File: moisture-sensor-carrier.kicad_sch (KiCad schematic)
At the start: 60 parts, among them J1 USB-C receptacle, J2 Battery - Adafruit 1578, J3 Solar panel, J4 SWD 10p 1.27mm, J5 U.FL-R-SMT-1(10) antenna, U1 nRF54L15-QFAA, U2 nPM1300-QEAA, U3 FDC1004, U4 SHT45-AD1F, U5 TPS7A1650 5V LDO, X1 CM8V-T1A 32.768kHz CL=7pF 20p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, X2 FA-128 32MHz CL=8pF

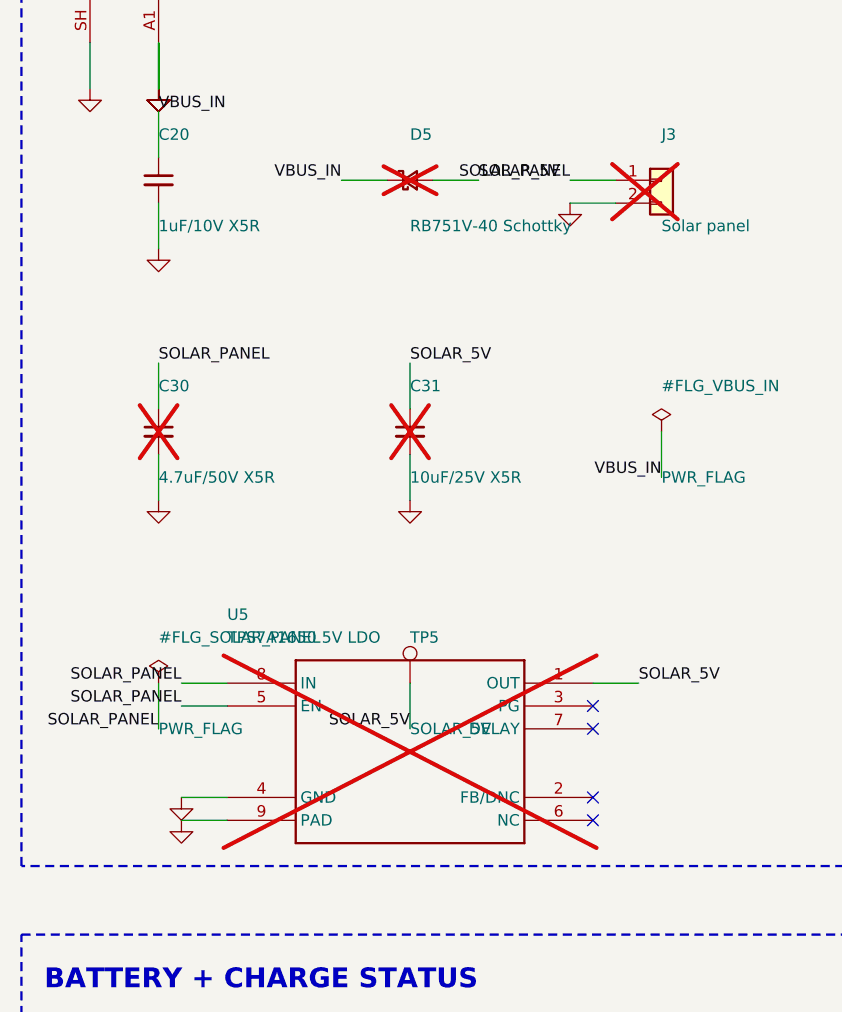
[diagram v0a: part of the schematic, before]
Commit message: Place U5/C30/C31 in the solar reserve; solar is populated on every board
Two changes.

SOLAR_DNP is now False. It was briefly DNP-by-default on the theory that most
units ship without a panel, but the parts are three passives and an LDO sitting
in space that was already reserved for them, and a populated board is upgraded by
plugging a panel in rather than by reworking one. J3, D5, U5, C30 and C31 are all
populated; nothing in the schematic carries a DNP flag.

U5, C30 and C31 are placed in the reserve below J3, in the Power-in band:

    U5   board x 24.37..30.63  y 50.75..54.25   HVSSOP-8, 6.26 x 3.50 courtyard
    C31  board x 23.85..27.15  y 48.27..49.73   output cap, nearest pin 1 (OUT)
    C30  board x 27.85..31.15  y 48.27..49.73   input cap,  nearest pin 8 (IN)

The block is 7.3 x 6.0 mm inside the ~8 x 8 mm that was set aside. Tightest
courtyard gap is 0.57 mm to J3, and it clears the board edge by 2.85 mm. The
caps sit on the side of U5 their pin is on - OUT is pins 1-4 on the left of the
HVSSOP, IN is 5-8 on the right - so neither return crosses the package. J3 and D5
did not move, which is what keeping the barrel jack off the board bought.

Pins 2, 3, 6 and 7 are left with no net, as the schematic has them: pin 2 is
FB/DNC and SBVS171F says do not route it to any electrical net, not even GND or
IN. References go on F.Fab like the rest of the board.

Unconnected 115 -> 124, all nine of them the new solar pads. NOT routed - the
solar nets join the general routing that is still outstanding.

One consequence worth flagging, recorded in LAYOUT.md section 10: with J3
populated on every board, the solar lead now has to enter the enclosure on every
board too. That is a THIRD wall penetration alongside the probe slot and the
SHT45 jut-out, and like those two it is unsealed unless potted.

ERC 0. DRC 0 errors, 4 isolated-copper warnings, 124 unconnected. DRU 16/16.
Schematic 60 components against 61 on the board - MP1 is board-only by design,
and nothing is schema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
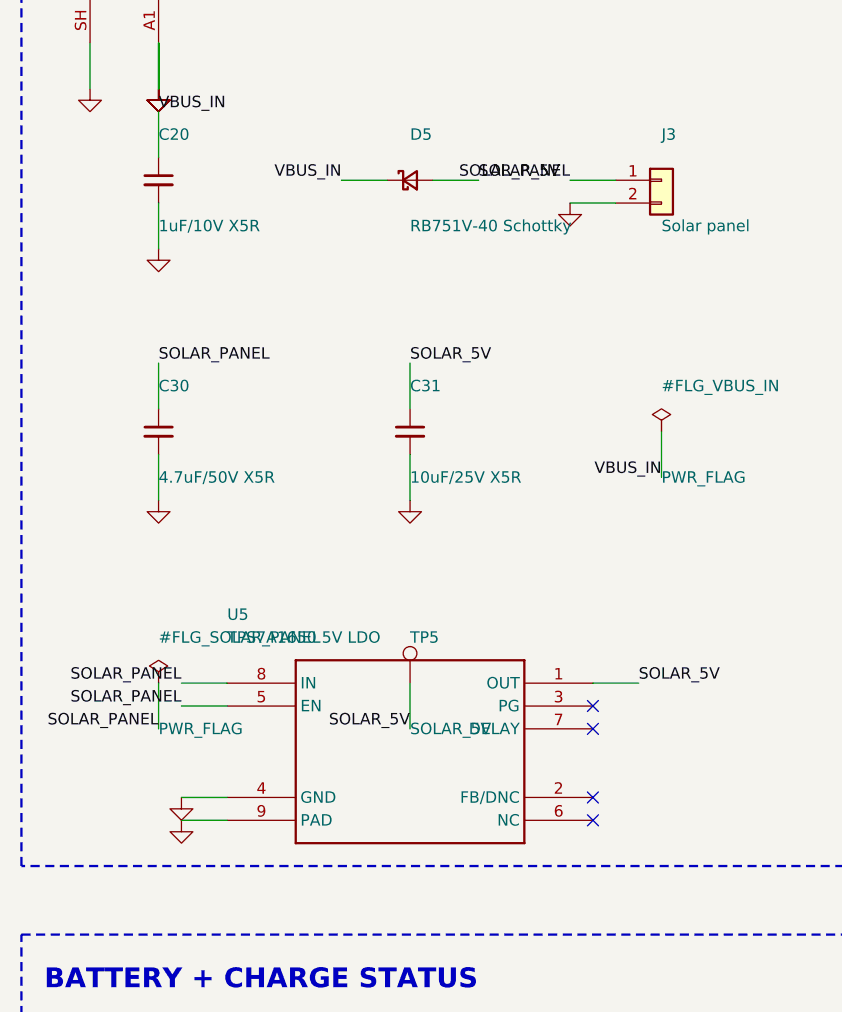
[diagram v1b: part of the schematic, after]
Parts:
- C30, C31, D5, J3, U5: now fitted
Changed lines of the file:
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@@
 		(in_bom yes)
 		(on_board yes)
-		(dnp yes)
+		(dnp no)
 		(fields_autoplaced yes)
 		(property "Reference" "D5"
@@
 		(in_bom yes)
 		(on_board yes)
-		(dnp yes)
+		(dnp no)
 		(fields_autoplaced yes)
 		(property "Reference" "J3"
@@
 		(in_bom yes)
 		(on_board yes)
-		(dnp yes)
+		(dnp no)
 		(fields_autoplaced yes)
 		(property "Reference" "C30"
@@
 		(in_bom yes)
 		(on_board yes)
-		(dnp yes)
+		(dnp no)
 		(fields_autoplaced yes)
 		(property "Reference" "C31"
@@
 		(in_bom yes)
 		(on_board yes)
-		(dnp yes)
+		(dnp no)
 		(fields_autoplaced yes)
 		(property "Reference" "U5"

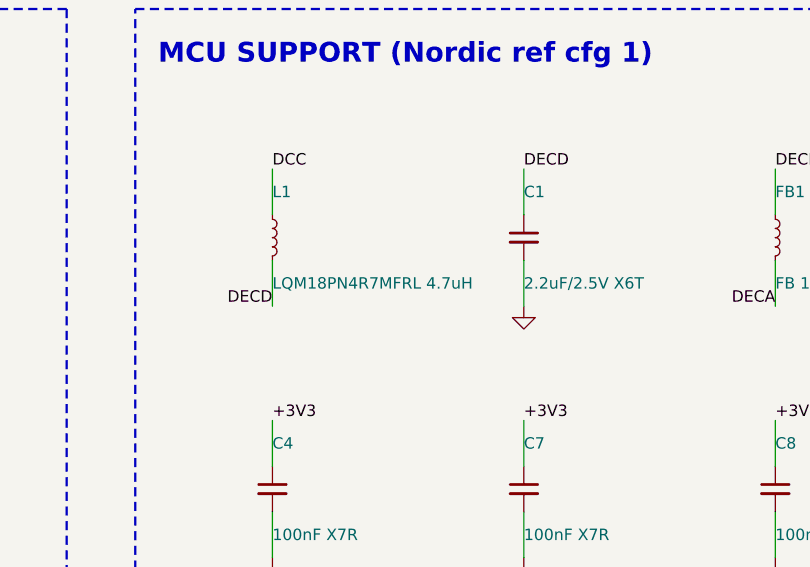
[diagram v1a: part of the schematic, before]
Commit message: L1 -> TDK MLZ1608M4R7WT000; the DC-bias question is closed, not deferred
L1 was the Murata LQM18PN4R7MFRL with a standing "pull the DC-bias curve from
SimSurfing before volume" note. That note should never have been left open, and
it is now closed by changing the part rather than by fetching a curve.

The Murata was chosen for margin: 620 mA rated against Nordic's 120 mA. But that
620 mA is a TEMPERATURE-RISE rating and Murata publishes no saturation current
at all for this part. In a buck, saturation is the parameter that decides
whether the thing is still an inductor; a thermal rating only says it will not
cook. The design was carrying a question that could not be answered from the
vendor's own data.

Two things settled it.

FIRST, Nordic's "requirement" is the TDK part's datasheet row. The nRF54L15
reference BOM lists L1 as 4.7 uH / 120 mA / +-20% / 650 mOhm / 0603. TDK's
MLZ1608M4R7WT000 row is 4.7 uH +-20%, DCR 0.5 Ohm +-30% (= 650 mOhm max),
Isat 120 mA, 1608 metric. All four match. So "the TDK lands exactly on two of
Nordic's numbers", which is why it lost the first time, is circular - those
numbers came from this part. It is not marginal against the spec, it IS the spec.
TDK also defines the rating precisely: "current assumed when inductance ratio has
decreased by 50% max", plus Itemp 350 mA typ. Both mechanisms specified.

SECOND, 120 mA is not a converter requirement anyway. The nRF54L15 REGULATORS
electrical specification (section 11.14) publishes recommended VDD and the
power-fail comparator thresholds and nothing else - no DC/DC peak inductor
current, no switching frequency. That is unlike the nPM1300, where Table 19
genuinely demands Isat > 350 mA because the hysteretic peak is set by the
converter and not by the load.

So the real question was what L1 actually carries. The buck steps VDD 3.3 V to
the 0.9 V DECD rail, and DECD feeds DECA/DECRF through FB1, so essentially all
active current goes through it:

    RX 1M/2M                      2.1 mA at V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
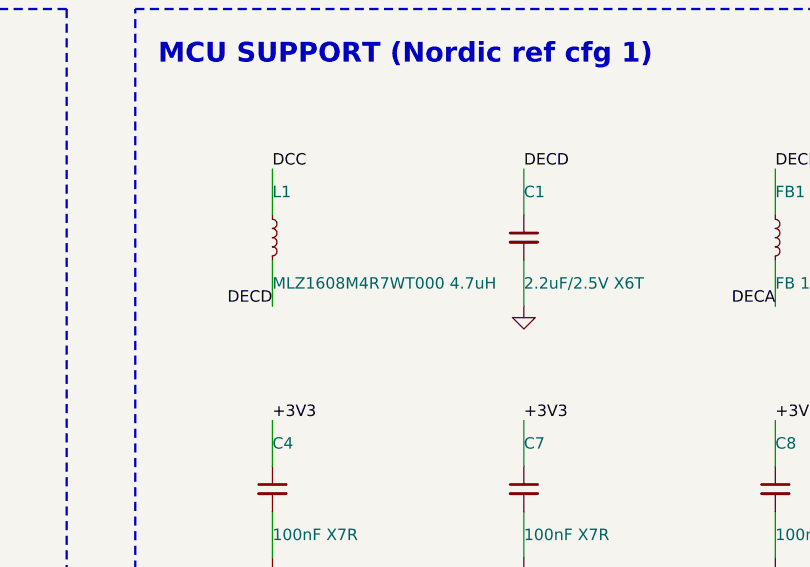
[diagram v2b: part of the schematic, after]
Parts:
- L1: value LQM18PN4R7MFRL 4.7uH -> MLZ1608M4R7WT000 4.7uH
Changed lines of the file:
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@@
 			(effects (font (size 1.27 1.27)) (justify left))
 		)
-		(property "Value" "LQM18PN4R7MFRL 4.7uH"
+		(property "Value" "MLZ1608M4R7WT000 4.7uH"
 			(at 368.3 220.98 0)
 			(effects (font (size 1.27 1.27)) (justify left))
